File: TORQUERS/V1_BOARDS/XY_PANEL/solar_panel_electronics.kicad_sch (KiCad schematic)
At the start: 34 parts, among them U3 LTC3130EUDC-1-PBF

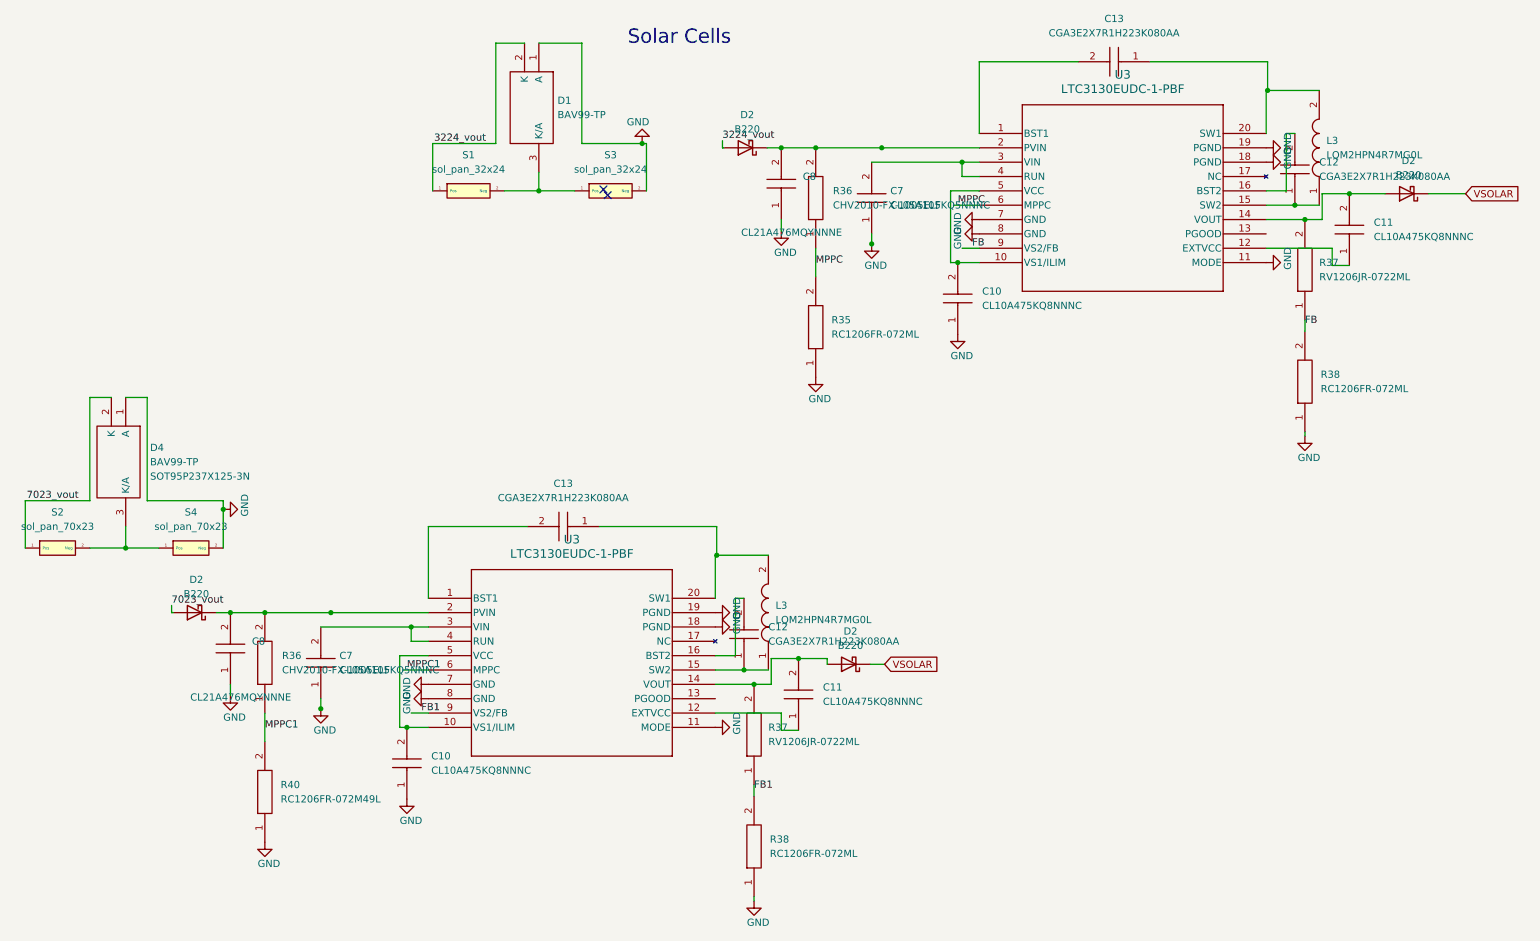
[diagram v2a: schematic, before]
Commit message: added buck for coil driver
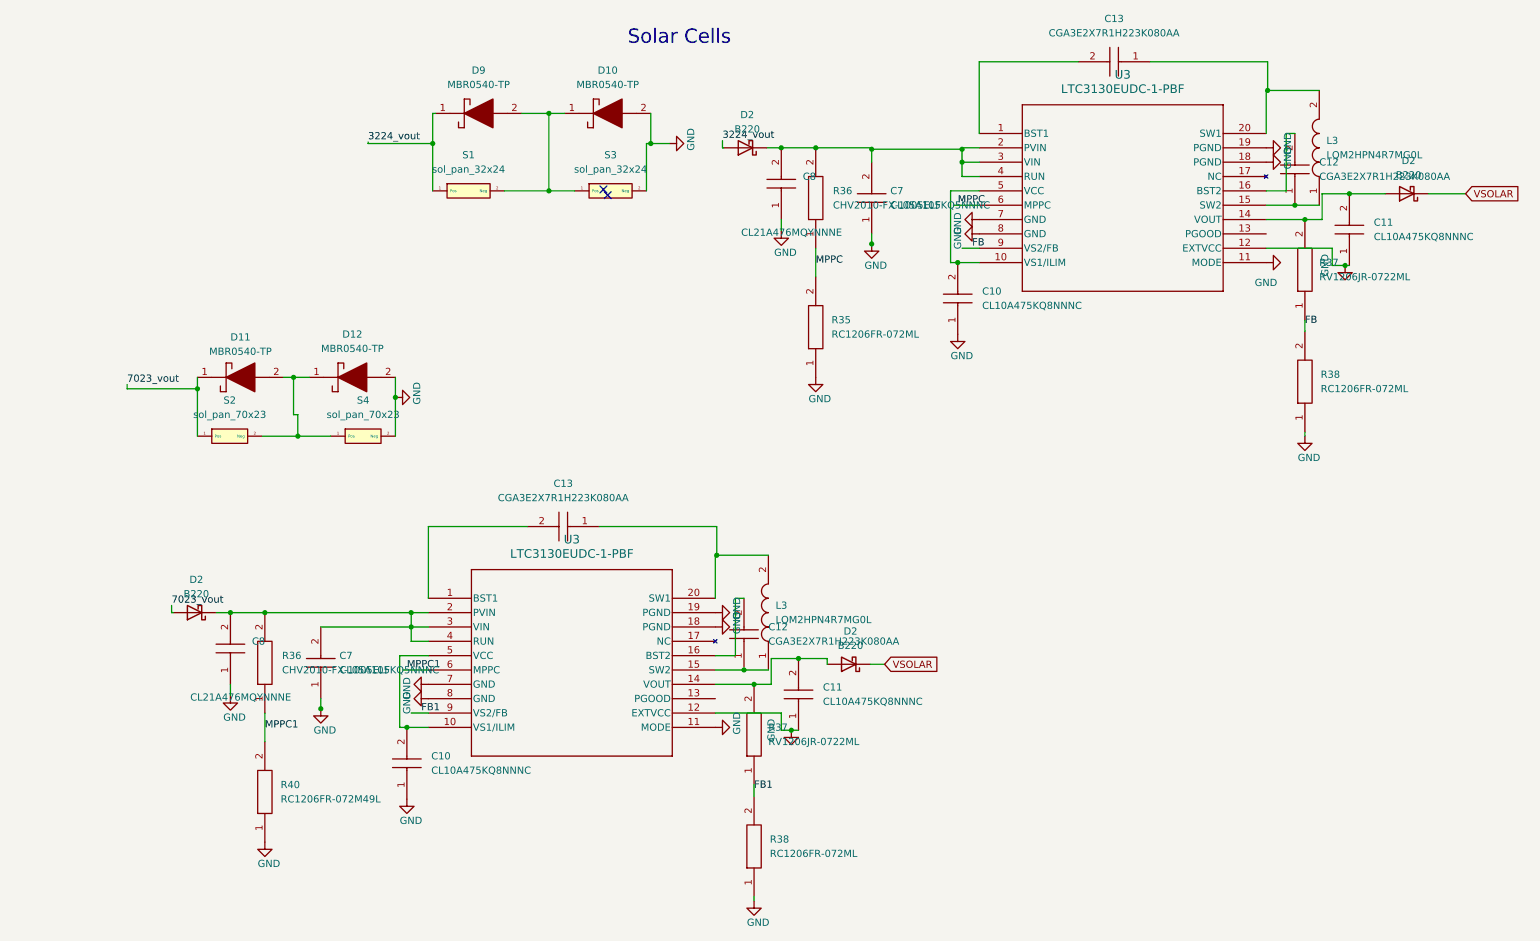
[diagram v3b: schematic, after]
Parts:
- removed D1, D4: BAV99-TP, SOT95P237X125-3N, symbol AA_AUTO_LOADER:BAV99-TP
- added D10, D11, D12, D9: MBR0540-TP, SOD3716X135N, symbol AA_AUTO_LOADER:MBR0540-TP
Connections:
- net 3224_vout: now also D9.1
- net 7023_vout: now also D11.1
- net GND: now also C11.1, C11.1, U3.12 (EXTVCC), U3.12 (EXTVCC), D10.2, D12.2
- net at C8.2, D2.1 (K), R36.2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: now also C7.2, U3.3 (VIN), U3.4 (RUN)
- net at C7.2, U3.3 (VIN), U3.4 (RUN): now also C8.2, D2.1 (K), R36.2, U3.2 (PVIN)
- net at S2.2 (Neg), S4.1 (Pos): now also D11.2, D12.1
- net at S1.2 (Neg), S3.1 (Pos): now also D10.1, D9.2
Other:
- moved on the sheet: S2, S4
